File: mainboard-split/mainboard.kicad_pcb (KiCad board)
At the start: 2 copper layers, 49.7 x 83.3 mm, 24 parts, among them J1 3V3 IN, J2 Conn_01x04, J3 Conn_01x03, J4 Conn_01x02, J5 3V3 OUT, J6 STICK POWER, SW1 SW_SPDT_MSM, SW2 SW_SPDT_MSM, SW3 SW_Push, SW4 SW_Push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

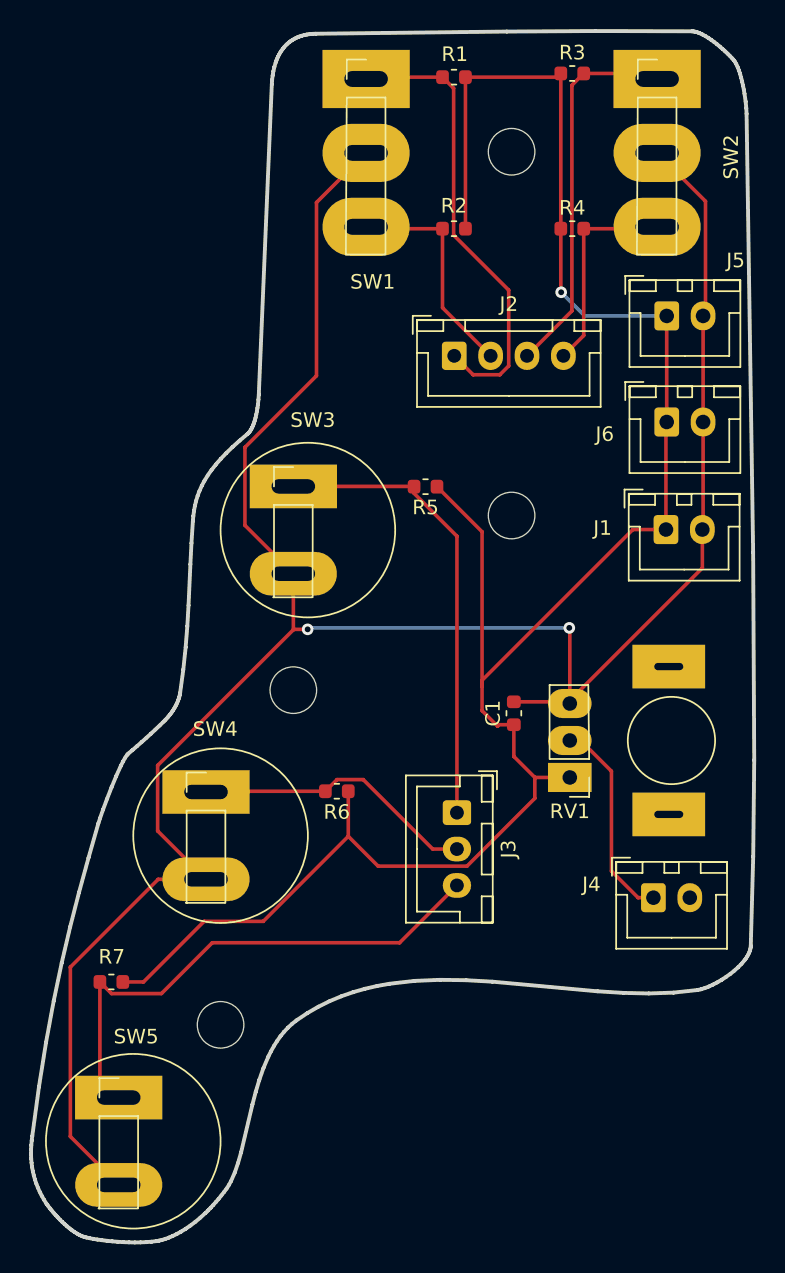
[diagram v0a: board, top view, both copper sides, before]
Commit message: Add fills.
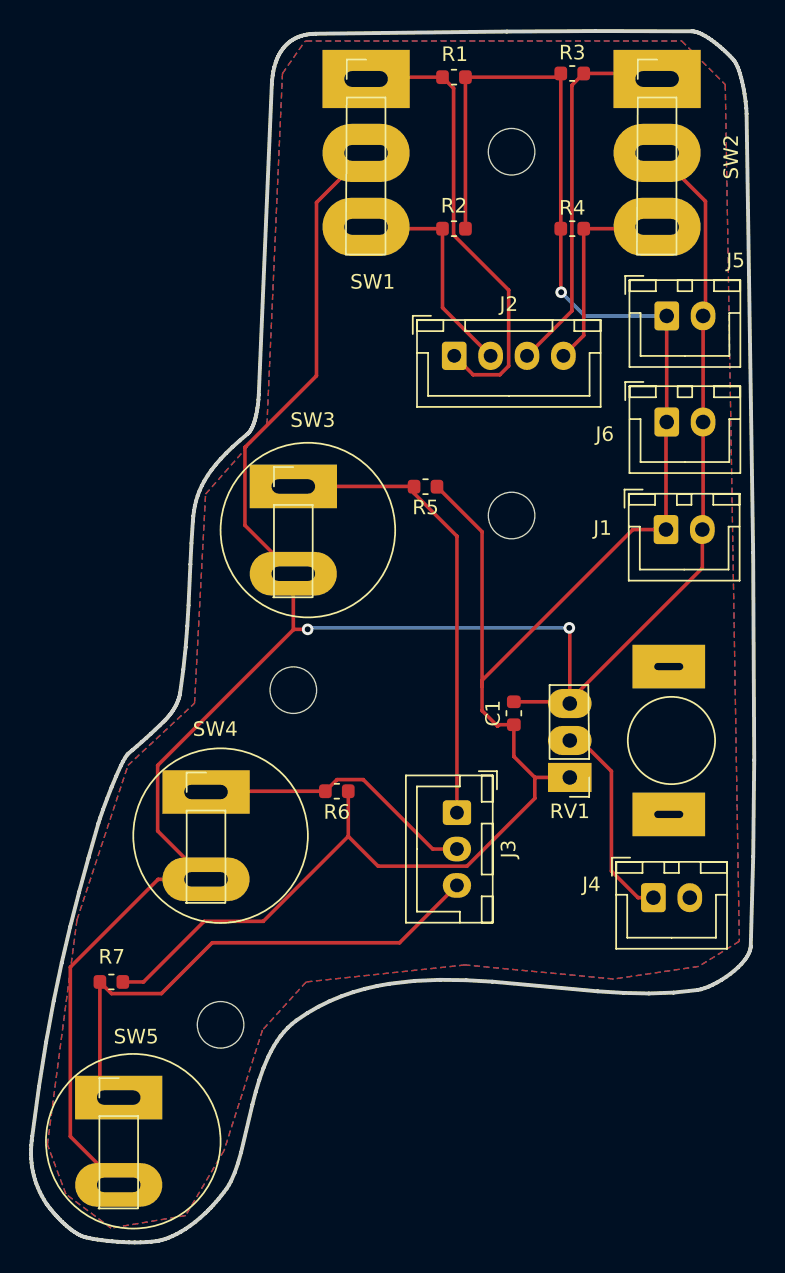
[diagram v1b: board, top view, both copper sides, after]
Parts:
- J1, J4, J5, J6: footprint Connector_JST:JST_XH_B2B-XH-A_1x02_P2.50mm_Vertical -> Connector_JST:JST_XH_B02B-XH-A_1x02_P2.50mm_Vertical
- J2: footprint Connector_JST:JST_XH_B4B-XH-A_1x04_P2.50mm_Vertical -> Connector_JST:JST_XH_B04B-XH-A_1x04_P2.50mm_Vertical
- J3: footprint Connector_JST:JST_XH_B3B-XH-A_1x03_P2.50mm_Vertical -> Connector_JST:JST_XH_B03B-XH-A_1x03_P2.50mm_Vertical
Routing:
- added copper zone on B.Cu, net GND
- added copper zone on F.Cu, net GND
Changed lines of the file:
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@@
 		)
 	)
-	(footprint "Connector_JST:JST_XH_B4B-XH-A_1x04_P2.50mm_Vertical"
+	(footprint "Connector_JST:JST_XH_B04B-XH-A_1x04_P2.50mm_Vertical"
 		(layer "F.Cu")
 		(at 66.0584 154.0256)
@@
 			)
 		)
-		(property "Footprint" "Connector_JST:JST_XH_B4B-XH-A_1x04_P2.50mm_Vertical"
+		(property "Footprint" "Connector_JST:JST_XH_B04B-XH-A_1x04_P2.50mm_Vertical"
 			(at 0 0 0)
 			(layer "F.Fab")
@@
 			(pintype "passive")
 		)
-		(model "${KICAD8_3DMODEL_DIR}/Connector_JST.3dshapes/JST_XH_B4B-XH-A_1x04_P2.50mm_Vertical.wrl"
+		(model "${KISYS3DMOD}/Connector_JST.3dshapes/JST_XH_B04B-XH-A_1x04_P2.50mm_Vertical.wrl"
 			(offset
 				(xyz 0 0 0)
@@
 		)
 	)
-	(footprint "Connector_JST:JST_XH_B2B-XH-A_1x02_P2.50mm_Vertical"
+	(footprint "Connector_JST:JST_XH_B02B-XH-A_1x02_P2.50mm_Vertical"
 		(layer "F.Cu")
 		(at 80.6088 165.9636)
@@
 			)
 		)
-		(property "Footprint" "Connector_JST:JST_XH_B2B-XH-A_1x02_P2.50mm_Vertical"
+		(property "Footprint" "Connector_JST:JST_XH_B02B-XH-A_1x02_P2.50mm_Vertical"
 			(at 0 0 0)
 			(layer "F.Fab")
@@
 		)
 	)
-	(footprint "Connector_JST:JST_XH_B3B-XH-A_1x03_P2.50mm_Vertical"
+	(footprint "Connector_JST:JST_XH_B03B-XH-A_1x03_P2.50mm_Vertical"
 		(layer "F.Cu")
 		(at 66.2432 185.42 -90)
@@
 		(tags "connector JST XH side entry")
 		(property "Reference" "J3"
-			(at 2.5 -3.55 90)
+			(at 2.5 -3.55 -90)
 			(layer "F.SilkS")
 			(effects
@@
 		)
 		(property "Value" "Conn_01x03"
-			(at 2.5 4.6 90)
+			(at 2.5 4.6 -90)
 			(layer "F.Fab")
 			(effects
@@
 			)
 		)
-		(property "Footprint" "Connector_JST:JST_XH_B3B-XH-A_1x03_P2.50mm_Vertical"
-			(at 0 0 90)
+		(property "Footprint" "Connector_JST:JST_XH_B03B-XH-A_1x03_P2.50mm_Vertical"
+			(at 0 0 -90)
 			(layer "F.Fab")
 			(hide yes)
@@
 		)
 		(property "Datasheet" ""
-			(at 0 0 90)
+			(at 0 0 -90)
 			(layer "F.Fab")
 			(hide yes)
@@
 		)
 		(property "Description" ""
-			(at 0 0 90)
+			(at 0 0 -90)
 			(layer "F.Fab")
 			(hide yes)
@@
 		)
 		(fp_text user "${REFERENCE}"
-			(at 2.5 2.7 90)
+			(at 2.5 2.7 -90)
 			(layer "F.Fab")
 			(effects
@@
 			(pintype "passive")
 		)
-		(model "${KICAD8_3DMODEL_DIR}/Connector_JST.3dshapes/JST_XH_B3B-XH-A_1x03_P2.50mm_Vertical.wrl"
+		(model "${KISYS3DMOD}/Connector_JST.3dshapes/JST_XH_B03B-XH-A_1x03_P2.50mm_Vertical.wrl"
 			(offset
 				(xyz 0 0 0)
@@
 		)
 	)
-	(footprint "Connector_JST:JST_XH_B2B-XH-A_1x02_P2.50mm_Vertical"
+	(footprint "Connector_JST:JST_XH_B02B-XH-A_1x02_P2.50mm_Vertical"
 		(layer "F.Cu")
 		(at 80.6596 158.5722)
@@
 			)
 		)
-		(property "Footprint" "Connector_JST:JST_XH_B2B-XH-A_1x02_P2.50mm_Vertical"
+		(property "Footprint" "Connector_JST:JST_XH_B02B-XH-A_1x02_P2.50mm_Vertical"
 			(at 0 0 0)
 			(layer "F.Fab")
@@
 		)
 	)
-	(footprint "Connector_JST:JST_XH_B2B-XH-A_1x02_P2.50mm_Vertical"
+	(footprint "Connector_JST:JST_XH_B02B-XH-A_1x02_P2.50mm_Vertical"
 		(layer "F.Cu")
 		(at 80.6596 151.2824)
@@
 			)
 		)
-		(property "Footprint" "Connector_JST:JST_XH_B2B-XH-A_1x02_P2.50mm_Vertical"
+		(property "Footprint" "Connector_JST:JST_XH_B02B-XH-A_1x02_P2.50mm_Vertical"
 			(at 0 0 0)
 			(layer "F.Fab")
@@
 		)
 	)
-	(footprint "Connector_JST:JST_XH_B2B-XH-A_1x02_P2.50mm_Vertical"
+	(footprint "Connector_JST:JST_XH_B02B-XH-A_1x02_P2.50mm_Vertical"
 		(layer "F.Cu")
 		(at 79.7452 191.262)
@@
 			)
 		)
-		(property "Footprint" "Connector_JST:JST_XH_B2B-XH-A_1x02_P2.50mm_Vertical"
+		(property "Footprint" "Connector_JST:JST_XH_B02B-XH-A_1x02_P2.50mm_Vertical"
 			(at 0 0 0)
 			(layer "F.Fab")
@@
 		(net 11)
 	)
+	(zone
+		(net 1)
+		(net_name "GND")
+		(layers "F&B.Cu")
+		(hatch edge 0.5)
+		(connect_pads
+			(clearance 0.508)
+		)
+		(min_thickness 0.25)
+		(filled_areas_thickness no)
+		(fill yes
+			(thermal_gap 0.5)
+			(thermal_bridge_width 0.5)
+		)
+		(polygon
+			(pts
+				(xy 55.88 132.3848) (xy 81.6864 132.3848) (xy 84.6836 135.382) (xy 85.6488 194.2592) (xy 82.8548 195.9864)
+				(xy 77.0128 196.85) (xy 66.802 195.8848) (xy 55.88 197.0532) (xy 52.8828 200.3552) (xy 50.2412 208.6356)
+				(xy 47.5996 213.106) (xy 42.4688 213.9696) (xy 39.37 211.6328) (xy 38.1 208.2292) (xy 40.132 192.786)
+				(xy 43.6372 182.1688) (xy 48.2092 177.9016) (xy 48.9712 163.5252) (xy 53.1876 158.75) (xy 54.2544 134.62)
+				(xy 55.7784 132.4356)
+			)
+		)
+	)
 	(group ""
